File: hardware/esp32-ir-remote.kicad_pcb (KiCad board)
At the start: 2 copper layers, 92 x 44 mm, 56 parts, among them J2 USB_C_Receptacle_USB2.0_14P, J4 GPIO_PWR, J5 EXT_IR, Q3 AO3400A, SW1 RESET, SW2 BOOT, U1 AMS1117-3.3, U3 ESP32-C3-WROOM-02, U4 TSOP382xx, U5 AHT20

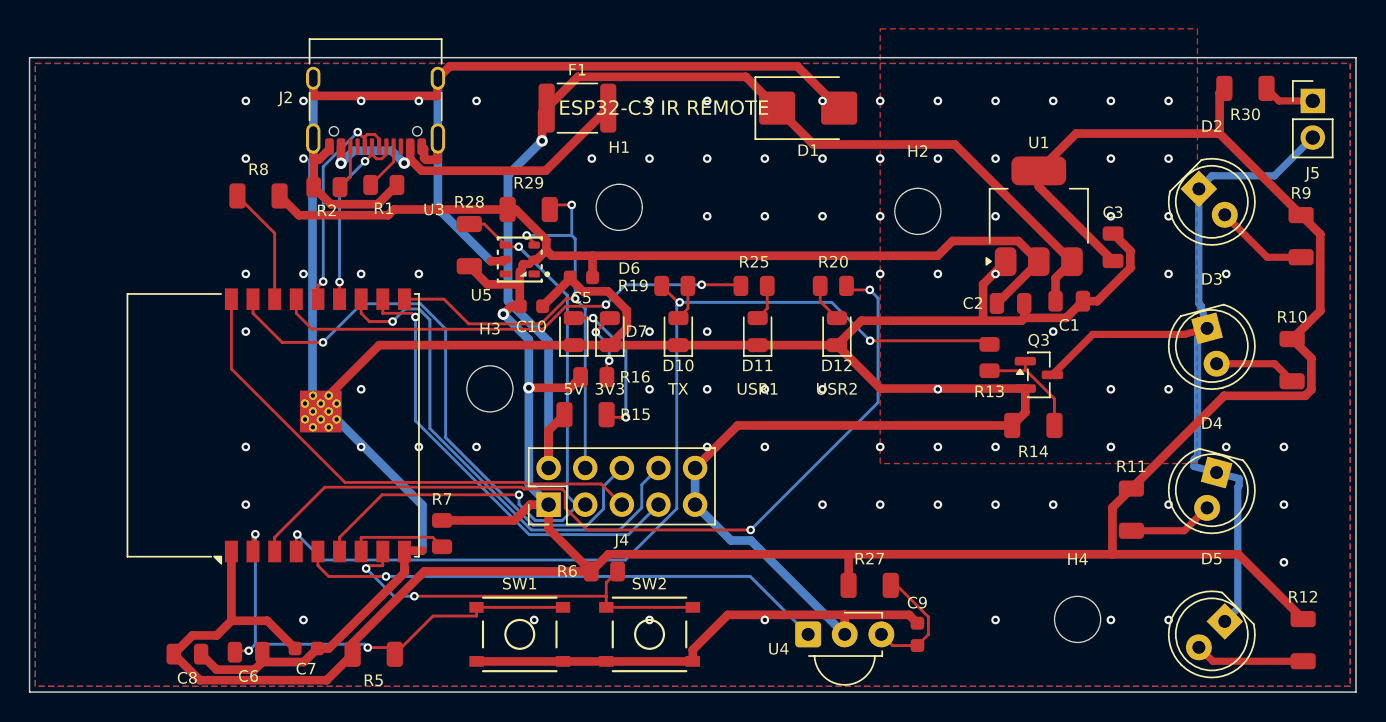
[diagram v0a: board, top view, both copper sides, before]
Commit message: hw(silk): re-home Layout-B silk — title off F1/D1, captions clear of R15/R16
The re-layout left two stale silk anchors: the board title's hardcoded home
(the old rot0 antenna strip, now F1/D1's pads on the N edge) and the fixed
caption row offset (Layout B seats R15/R16 directly under the D6/D7 LEDs).

pcb_silk.py placement made layout-proof rather than re-hardcoded:
- title moved to the scanned pad-free band S of D1 (156.75, 79)
- captions pick the first clear offset: uniform row preferred, then per-LED
  sideways/down nudges bounded to half the LED pitch (a caption that drifts
  further actively mislabels the neighbour), vertical as a last resort
  ('5V' slots vertically between H3 and R16)
- real stroke-font extents (measured 1.07*len*size x 1.61*size; the old
  0.75 estimate under-read ~35% and let refs land on LED outlines)
- footprint silk outlines join the obstacle list (kills ref-on-LED-bar)
- status LEDs get NO silk ref: cluster too dense, the placer scattered
  D10/D11/D12 refs into wrong-reading spots; the function caption is the
  curated label (refs live in iBOM/fab docs)

DRC: silk_overlap 2->0, silk_over_copper 5->0; 0 unconnected; electrically
untouched (silk/text only). 4x hole_clearance are KiCad 10.0.4-only
same-footprint NPTH checks on J2 (CI's pinned 10.0.2 reports 0).

Co-Authored-By: Claude Fable 5 <noreply@anthropic.com>
Claude-Session: https://claude.ai/code/session_01LTcYEfzEh7d6xWh7GWNhrd
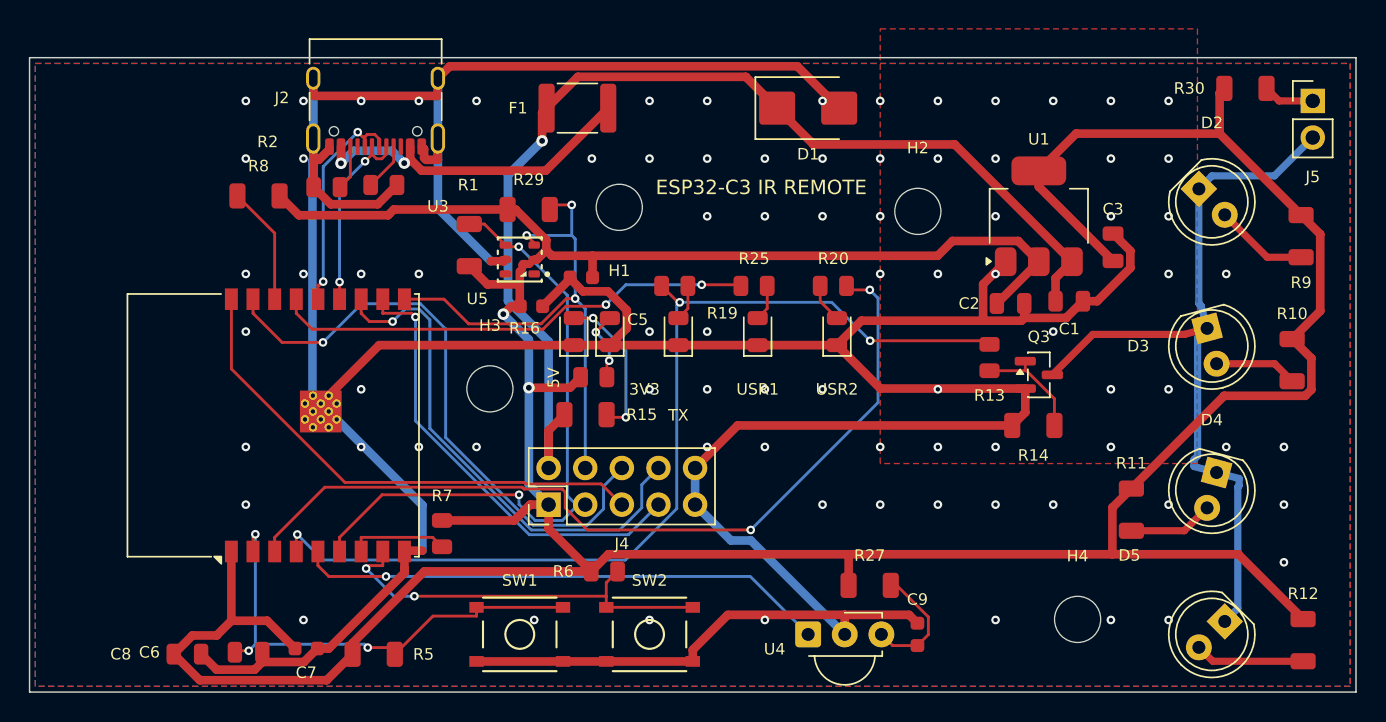
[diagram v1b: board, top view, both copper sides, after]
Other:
- board text added: "2026-06-16 git 74b508b-dirty"
- board text removed: "2026-06-16 git 3b077d0-dirty"
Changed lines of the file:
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@@
 		(tags "resistor")
 		(property "Reference" "R1"
-			(at 0 1.645 0)
+			(at 5.854999 0 0)
 			(layer "F.SilkS")
 			(effects
@@
 		(tags "component")
 		(property "Reference" "U5"
-			(at -2.665 2.475 0)
+			(at -2.945 2.723 0)
 			(layer "F.SilkS")
 			(effects
@@
 		(tags "SOT TO_SOT_SMD")
 		(property "Reference" "Q3"
-			(at 0 -2.395 0)
+			(at 0 -2.643 0)
 			(layer "F.SilkS")
 			(effects
@@
 		(tags "capacitor")
 		(property "Reference" "C5"
-			(at 0 1.424999 0)
+			(at 3.905 2.923 0)
 			(layer "F.SilkS")
 			(effects
@@
 		(tags "mountinghole M3")
 		(property "Reference" "H2"
-			(at 0.001264 -4.147526 0)
+			(at 0.001264 -4.395526 0)
 			(layer "F.SilkS")
 			(effects
@@
 		(tags "LED")
 		(property "Reference" "D4"
-			(at -3.197368 1.198368 0)
+			(at -3.436918 1.262555 0)
 			(layer "F.SilkS")
 			(effects
@@
 		(tags "resistor")
 		(property "Reference" "R12"
-			(at 2.975 0 0)
+			(at 3.223 0 0)
 			(layer "F.SilkS")
 			(effects
@@
 		(tags "resistor")
 		(property "Reference" "R9"
-			(at 2.975 0 0)
+			(at -3.223 0 0)
 			(layer "F.SilkS")
 			(effects
@@
 		(tags "resistor")
 		(property "Reference" "R5"
-			(at 0 1.825 0)
+			(at 3.455 0 0)
 			(layer "F.SilkS")
 			(effects
@@
 		(tags "resistor")
 		(property "Reference" "R25"
-			(at 0 -1.645 0)
+			(at 0 -1.893 0)
 			(layer "F.SilkS")
 			(effects
@@
 		(tags "resistor")
 		(property "Reference" "R19"
-			(at -2.875 0 0)
+			(at 3.295 1.893 0)
 			(layer "F.SilkS")
 			(effects
@@
 		(tags "resistor")
 		(property "Reference" "R11"
-			(at 2.975 0 0)
+			(at 3.223 0 0)
 			(layer "F.SilkS")
 			(effects
@@
 		(tags "capacitor")
 		(property "Reference" "C2"
-			(at -2.595 0 0)
+			(at -2.875 0 0)
 			(layer "F.SilkS")
 			(effects
@@
 		(tags "LED")
 		(property "Reference" "D12"
-			(at -2.375 0 0)
+			(at 0 -2.565 0)
 			(layer "F.SilkS")
+			(hide yes)
 			(effects
 				(font
@@
 		(tags "mountinghole M3")
 		(property "Reference" "H4"
-			(at 0.001264 -4.147526 0)
+			(at 0.001264 -4.395527 0)
 			(layer "F.SilkS")
 			(effects
@@
 		(tags "LED")
 		(property "Reference" "D6"
-			(at 4.375 3.845 0)
+			(at 8.123 7.625 0)
 			(layer "F.SilkS")
+			(hide yes)
 			(effects
 				(font
@@
 		(tags "resistor")
 		(property "Reference" "R8"
-			(at 0 -1.825 0)
+			(at 0 -2.073 0)
 			(layer "F.SilkS")
 			(effects
@@
 		(tags "tact switch TS-1187A C318884")
 		(property "Reference" "SW1"
-			(at 0 -3.495 0)
+			(at 0 -3.743 0)
 			(layer "F.SilkS")
 			(effects
@@
 		(tags "fuse")
 		(property "Reference" "F1"
-			(at 0 -2.645 0)
+			(at -4.125 0 0)
 			(layer "F.SilkS")
 			(effects
@@
 		(tags "resistor")
 		(property "Reference" "R30"
-			(at 0 1.825 0)
+			(at -3.895 0 0)
 			(layer "F.SilkS")
 			(effects
@@
 		(tags "LED")
 		(property "Reference" "D5"
-			(at -2.427475 3.702476 0)
+			(at 1.439048 7.919724 0)
 			(layer "F.SilkS")
 			(effects
@@
 			(at 2.975 0 0)
 			(layer "F.SilkS")
+			(hide yes)
 			(effects
 				(font
@@
 		(tags "capacitor")
 		(property "Reference" "C7"
-			(at 0 1.425 0)
+			(at 0 1.673 0)
 			(layer "F.SilkS")
 			(effects
@@
 		(tags "resistor")
 		(property "Reference" "R27"
-			(at 0 -1.825001 0)
+			(at 0 -2.073001 0)
 			(layer "F.SilkS")
 			(effects
@@
 		(tags "LED")
 		(property "Reference" "D2"
-			(at -2.427475 -3.702473 0)
+			(at -2.602837 -3.877836 0)
 			(layer "F.SilkS")
 			(effects
@@
 		(tags "LED")
 		(property "Reference" "D7"
-			(at 0 1.845 0)
+			(at 5.623 5.125 0)
 			(layer "F.SilkS")
+			(hide yes)
 			(effects
 				(font
@@
 		(tags "resistor")
 		(property "Reference" "R14"
-			(at 0 1.825 0)
+			(at 0 2.073 0)
 			(layer "F.SilkS")
 			(effects
@@
 		(tags "IR Receiver Vishay TSOP-xxxx MINICAST")
 		(property "Reference" "U4"
-			(at -2.045001 1.025 0)
+			(at -2.325001 1.025 0)
 			(layer "F.SilkS")
 			(effects
@@
 		(tags "Diode SMB (DO-214AA)")
 		(property "Reference" "D1"
-			(at 0 2.945 0)
+			(at 0 3.193 0)
 			(layer "F.SilkS")
 			(effects
@@
 		(tags "LED")
 		(property "Reference" "D11"
-			(at -2.375 0 0)
+			(at -3.373 -3.315 0)
 			(layer "F.SilkS")
+			(hide yes)
 			(effects
 				(font
@@
 		(tags "ESP32-C3 WROOM-02 espressif")
 		(property "Reference" "U3"
-			(at 14.945 8.045 0)
+			(at 15.193 8.325 0)
 			(layer "F.SilkS")
 			(effects
@@
 		(tags "capacitor")
 		(property "Reference" "C9"
-			(at 2.175 0 0)
+			(at 2.423 0 0)
 			(layer "F.SilkS")
 			(effects
@@
 		(tags "resistor")
 		(property "Reference" "R2"
-			(at 0 1.645 0)
+			(at -4.105 -3.143 0)
 			(layer "F.SilkS")
 			(effects
@@
 		(tags "tact switch TS-1187A C318884")
 		(property "Reference" "SW2"
-			(at 0 -3.495 0)
+			(at 0 -3.743 0)
 			(layer "F.SilkS")
 			(effects
@@
 		(tags "LED")
 		(property "Reference" "D10"
-			(at -2.375 0 0)
+			(at -5.623 5.565 0)
 			(layer "F.SilkS")
+			(hide yes)
 			(effects
 				(font
@@
 		(tags "CMS SOT")
 		(property "Reference" "U1"
-			(at 5.095 0 0)
+			(at 5.343 0 0)
 			(layer "F.SilkS")
 			(effects
@@
 		(tags "Through hole pin header THT 2x05 2.54mm double row")
 		(property "Reference" "J4"
-			(at -2.464999 5.08 0)
+			(at -2.713 5.08 0)
 			(layer "F.SilkS")
 			(effects
@@
 		(tags "resistor")
 		(property "Reference" "R7"
-			(at 2.375 0 0)
+			(at 2.623 0 0)
 			(layer "F.SilkS")
 			(effects
@@
 		(tags "capacitor")
 		(property "Reference" "C1"
-			(at 0 1.675 0)
+			(at 0 1.923 0)
 			(layer "F.SilkS")
 			(effects
@@
 		(tags "capacitor")
 		(property "Reference" "C3"
-			(at 2.395 0 0)
+			(at 2.643 0 0)
 			(layer "F.SilkS")
 			(effects
@@
 		(tags "resistor")
 		(property "Reference" "R13"
-			(at -2.375 0 0)
+			(at -2.623 0 0)
 			(layer "F.SilkS")
 			(effects
@@
 		(tags "capacitor")
 		(property "Reference" "C6"
-			(at 0 1.674999 0)
+			(at -6.875 0 0)
 			(layer "F.SilkS")
 			(effects
@@
 		(tags "capacitor")
 		(property "Reference" "C8"
-			(at 0 1.675 0)
+			(at -4.625 0 0)
 			(layer "F.SilkS")
 			(effects
@@
 		(tags "resistor")
 		(property "Reference" "R29"
-			(at 0 -1.825 0)
+			(at 0 -2.073 0)
 			(layer "F.SilkS")
 			(effects
@@
 		(tags "mountinghole M3")
 		(property "Reference" "H3"
-			(at 0.001264 -4.147526 0)
+			(at 0.001264 -4.395526 0)
 			(layer "F.SilkS")
 			(effects
@@
 		(tags "mountinghole M3")
 		(property "Reference" "H1"
-			(at 0.001264 -4.147526 0)
+			(at 0.001264 4.395526 0)
 			(layer "F.SilkS")
 			(effects
@@
 		(tags "resistor")
 		(property "Reference" "R10"
-			(at 2.975 0 0)
+			(at 3.223 0 0)
 			(layer "F.SilkS")
 			(effects
@@
 		(tags "Through hole pin header THT 1x02 2.54mm single row")
 		(property "Reference" "J5"
-			(at 0 5.015 0)
+			(at 0 5.263 0)
 			(layer "F.SilkS")
 			(effects
@@
 		(tags "resistor")
 		(property "Reference" "R16"
-			(at 2.875 0 0)
+			(at -4.795 -3.393 0)
 			(layer "F.SilkS")
 			(effects
@@
 		(tags "resistor")
 		(property "Reference" "R20"
-			(at 0 -1.645 0)
+			(at 0 -1.893 0)
 			(layer "F.SilkS")
 			(effects
@@
 		(tags "LED")
 		(property "Reference" "D3"
-			(at -3.197369 -1.198365 0)
+			(at -0.046686 4.932599 0)
 			(layer "F.SilkS")
 			(effects
@@
 		(tags "resistor")
 		(property "Reference" "R6"
-			(at -2.575 0 0)
+			(at -2.855 0 0)
 			(layer "F.SilkS")
 			(effects
@@
 		(tags "USB C Type-C Receptacle SMD")
 		(property "Reference" "J2"
-			(at 6.215 -0.285 0)
+			(at 6.495 -0.285 0)
 			(layer "F.SilkS")
 			(effects
@@
 			(at 0 1.424999 0)
 			(layer "F.SilkS")
+			(hide yes)
 			(effects
 				(font
@@
 		(tags "resistor")
 		(property "Reference" "R15"
-			(at 3.475 0 0)
+			(at 3.895 0 0)
 			(layer "F.SilkS")
 			(effects
@@
 		(layer "Edge.Cuts")
 	)
-	(gr_text "5V"
-		(at 143.75 93 0)
+	(gr_text "3V3"
+		(at 148.65 93 0)
 		(layer "F.SilkS")
 		(effects
@@
 		)
 	)
-	(gr_text "3V3"
-		(at 146.25 93 0)
+	(gr_text "TX"
+		(at 151 94.8 0)
 		(layer "F.SilkS")
 		(effects
@@
 		)
 	)
-	(gr_text "TX"
-		(at 151 93 0)
+	(gr_text "USR1"
+		(at 156.5 93 0)
 		(layer "F.SilkS")
 		(effects
@@
 		)
 	)
-	(gr_text "USR1"
-		(at 156.5 93 0)
+	(gr_text "USR2"
+		(at 162 93 0)
 		(layer "F.SilkS")
 		(effects
@@
 		)
 	)
-	(gr_text "USR2"
-		(at 162 93 0)
+	(gr_text "5V"
+		(at 142.35 92.2 90)
 		(layer "F.SilkS")
 		(effects
@@
 	)
 	(gr_text "ESP32-C3 IR REMOTE"
-		(at 150 73.5 0)
+		(at 156.75 79 0)
 		(layer "F.SilkS")
 		(effects
@@
 		)
 	)
-	(gr_text "2026-06-16  git 3b077d0-dirty"
+	(gr_text "2026-06-16  git 74b508b-dirty"
 		(at 152 91.4 0)
 		(layer "B.SilkS")
